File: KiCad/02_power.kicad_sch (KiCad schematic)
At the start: 0 parts

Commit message: Update power scheme
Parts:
- added C100, C101, C102, C103, C203, C204: 2.2uF, Capacitor_SMD:C_0603_1608Metric, symbol Device:C
- added C104: DNP, Capacitor_SMD:C_0603_1608Metric, symbol Device:C
- added C205, C206: 22uF, Capacitor_SMD:C_0603_1608Metric, symbol Device:C
- added C207, C208: 100nF, Capacitor_SMD:C_0603_1608Metric, symbol Device:C
- added C209, C500: 10uF, Capacitor_SMD:C_0603_1608Metric, symbol Device:C
- added D100, D101: LED, LED_SMD:LED_0603_1608Metric, symbol Device:LED
- added D201, D202, D203: 1N5819HW-7-F, Diode_SMD:D_SOD-123, symbol Device:D_Schottky
- added F100, F101, F201: 3A, Fuse:Fuse_0805_2012Metric, symbol Device:Polyfuse
- added FB100, FB101, FB201: 120R, Fuse:Fuse_0603_1608Metric, symbol Device:FerriteBead
- added J100: Barrel_Jack_Switch_Pin3Ring, Connector_BarrelJack:BarrelJack_GCT_DCJ200-10-A_Horizontal, symbol Connector:Barrel_Jack_Switch_Pin3Ring
- added L101: 15uH, esp32_s3_weather_webserver:MWSA0603S, symbol Device:L
- added R100: 100kR, Resistor_SMD:R_0805_2012Metric, symbol Device:R
- added R101: 22kR, Resistor_SMD:R_0805_2012Metric, symbol Device:R
- added R102, R201: 510R, Resistor_SMD:R_0402_1005Metric, symbol Device:R
- added U100: TLV62569DBV, Package_TO_SOT_SMD:SOT-23-5, symbol Regulator_Switching:TLV62569DBV
- added U201: AMS1117-3.3, Package_TO_SOT_SMD:SOT-223-3_TabPin2, symbol Regulator_Linear:AMS1117-3.3
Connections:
- new net +3V3: C208.1, C209.1, R201.2, U201.2 (VO)
- new net +3V3_PER: C104.1, C206.1, L101.2, R100.2, R102.2
- new net +5V: C205.1, C207.1, C500.1, D201.1 (K), D202.1 (K), D203.1 (K), U100.1 (EN), U100.4 (VIN), U201.3 (VI)
- new net +5V_IN: F100.1, J100.1
- new net +5V_IN_FILT: C101.1, D201.2 (A), FB100.1
- new net +5V_IN_FUSE: C100.1, F100.2, FB100.2
- new net +VCC_USB2UART_FILT: C103.1, D202.2 (A), FB101.1
- new net +VCC_USB2UART_FUSE: C102.1, F101.2, FB101.2
- new net +VCC_USB_FILT: C204.1, D203.2 (A), FB201.1
- new net +VCC_USB_FUSE: C203.1, F201.2, FB201.2
- new net BUCK_FB: C104.2, R100.1, R101.2, U100.5 (FB)
- new net BUCK_SW: L101.1, U100.3 (SW)
- new net GND: C100.2, C101.2, C102.2, C103.2, C203.2, C204.2, C205.2, C206.2, C207.2, C208.2, C209.2, C500.2, D100.1 (K), D101.1 (K), J100.2, J100.3, R101.1, U100.2 (GND), U201.1 (GND)
- new net LED_3V3_A: D100.2 (A), R201.1
- new net LED_3V3_PER_A: D101.2 (A), R102.1
- new net USB2UART_VBUS: F101.1
- new net USB_VBUS: F201.1
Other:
- note added: "I(load)=0.25A max"
- note added: "Power indication"
- note added: "Power input"
- note added: "Powering ESP32"
- note added: "Powering Peripherals"
- note added: "V(out)=0.6*(1+100k/22k)=3.327V"
- note added: "WEBENCH Tools"
- note added: "[2] Power"
- note added: "f(sw)=1.5MHz"

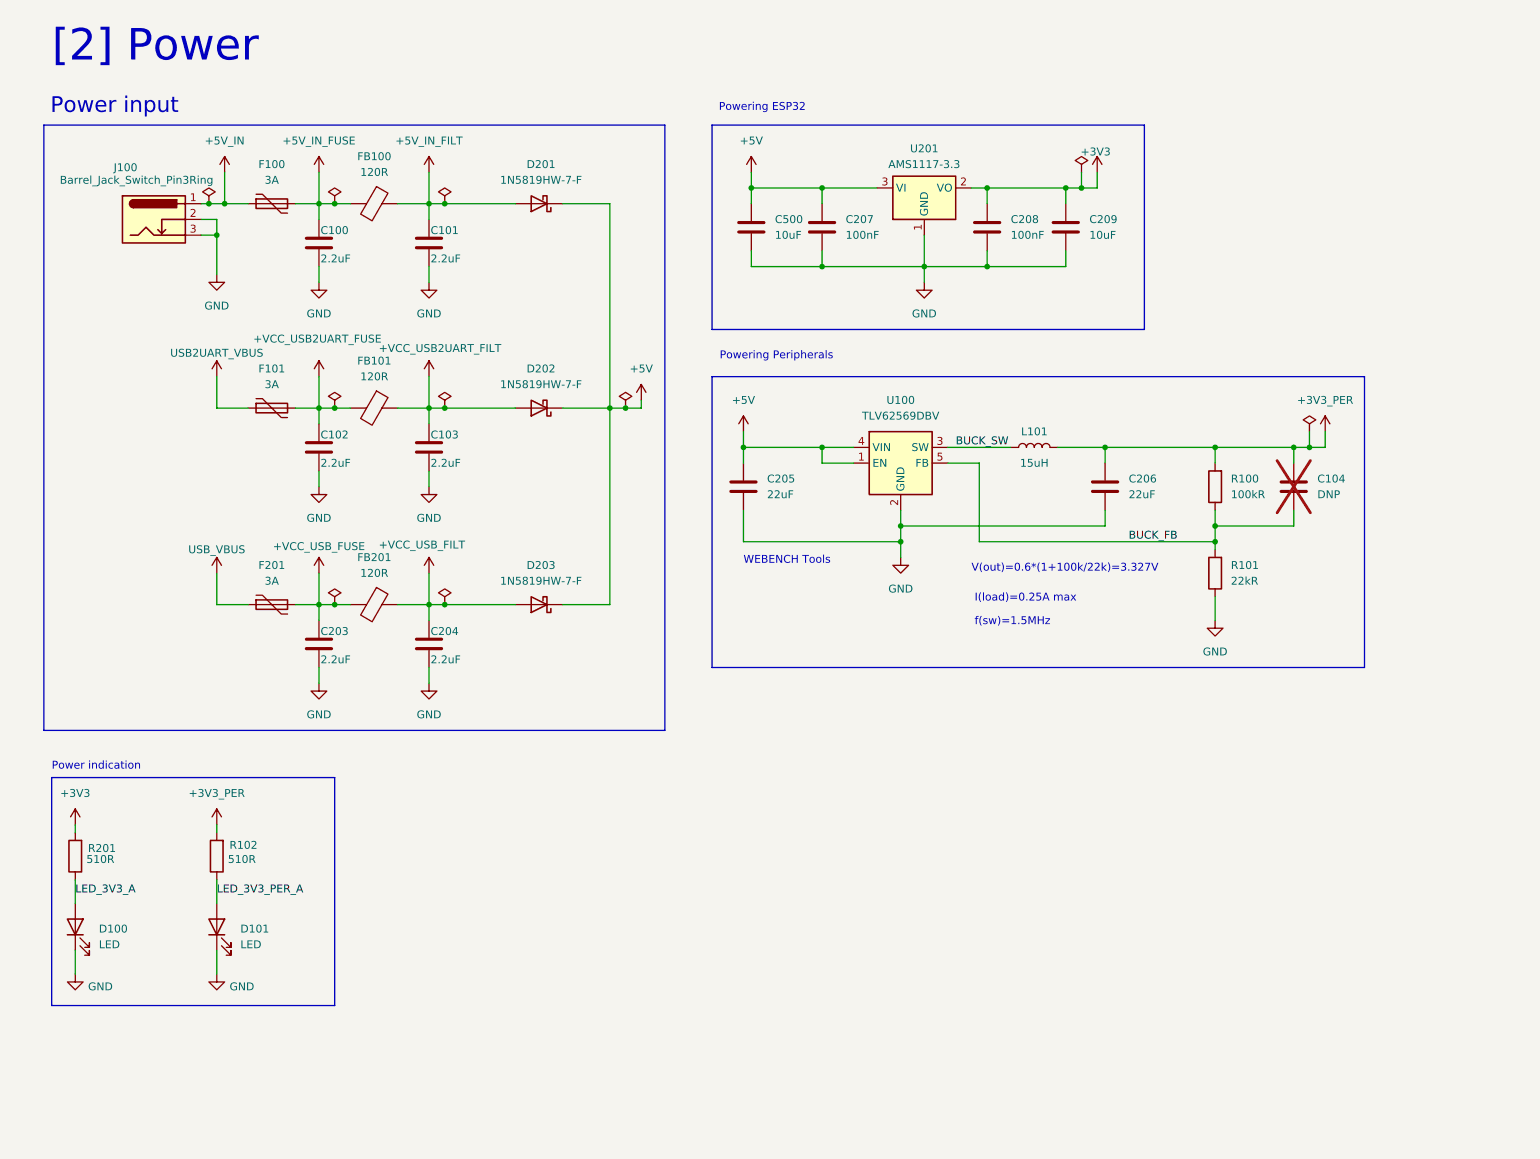
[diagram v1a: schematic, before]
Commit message: Add analog sensors
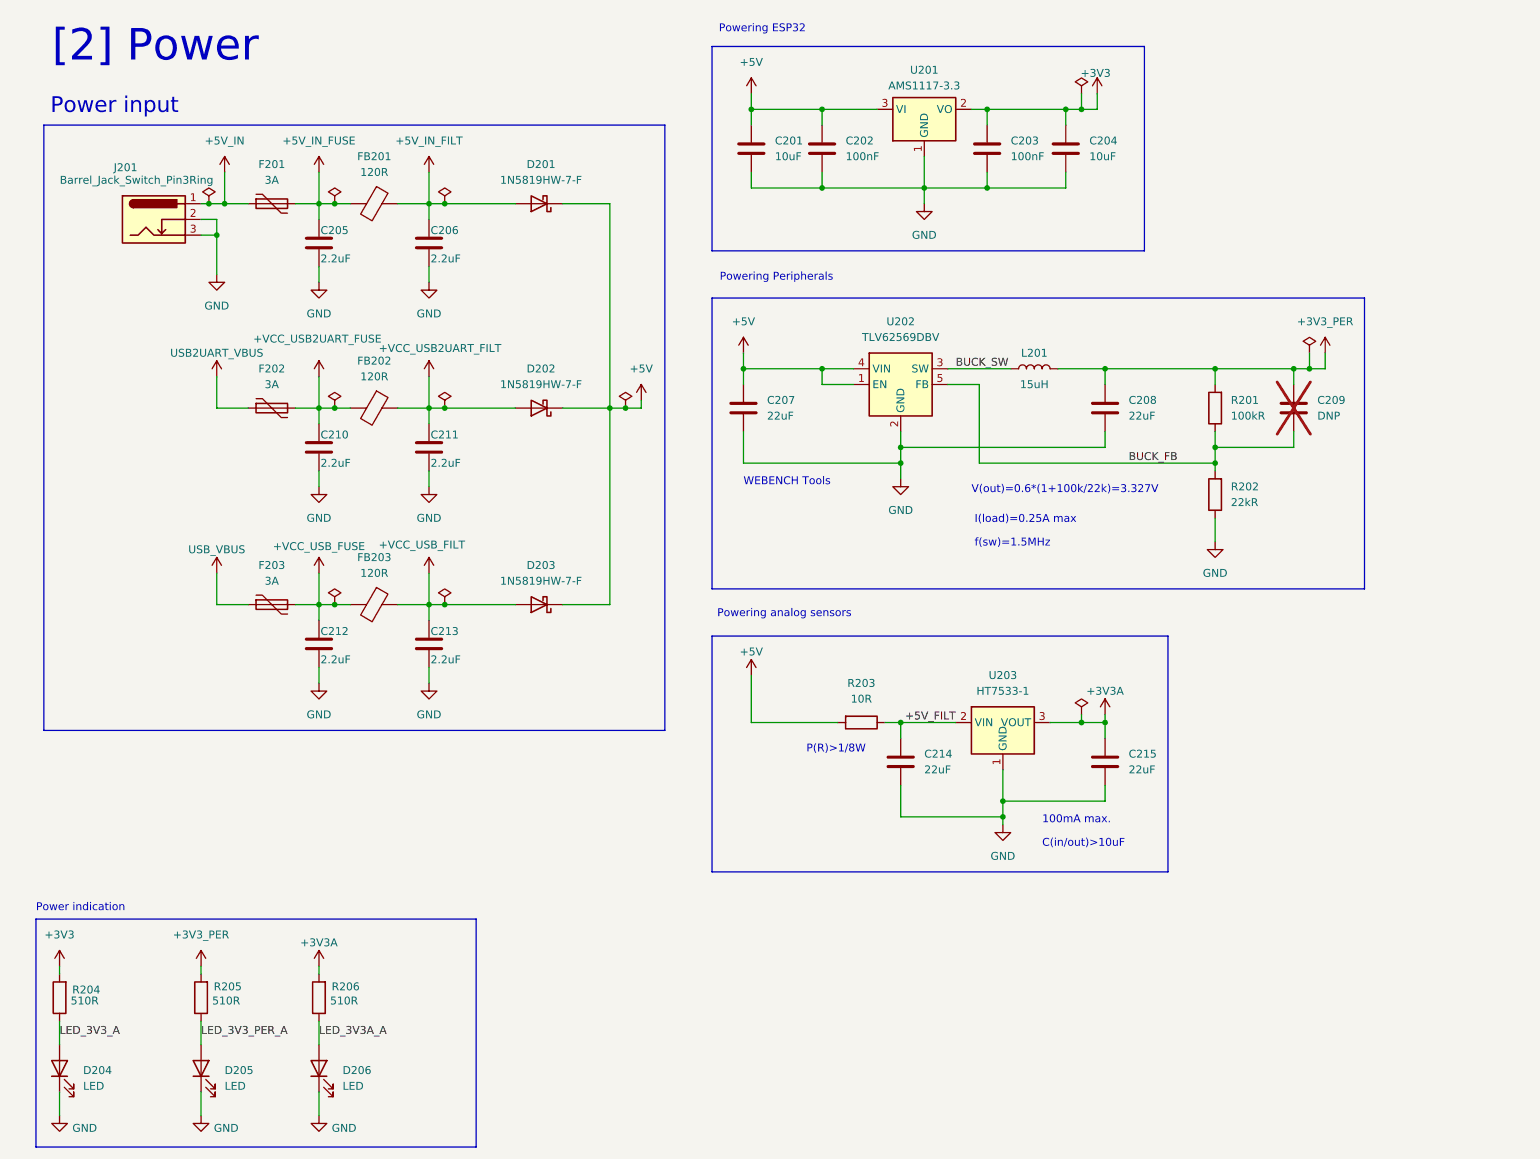
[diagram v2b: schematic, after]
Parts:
- added C214, C215: 22uF, Capacitor_SMD:C_0805_2012Metric, symbol Device:C
- added D206: LED, LED_SMD:LED_0603_1608Metric, symbol Device:LED
- added R203: 10R, Resistor_SMD:R_0805_2012Metric, symbol Device:R
- added R206: 510R, Resistor_SMD:R_0402_1005Metric, symbol Device:R
- added U203: HT7533-1, Package_TO_SOT_SMD:SOT-89-3, symbol Regulator_Linear:HT75xx-1-SOT89
- renumbered C500 to C201, C207 to C202, C208 to C203, C209 to C204, C100 to C205, C101 to C206, C205 to C207, C206 to C208, C104 to C209, C102 to C210, C103 to C211, C203 to C212, C204 to C213, D100 to D204, D101 to D205, F100 to F201, F101 to F202, F201 to F203, FB100 to FB201, FB101 to FB202, FB201 to FB203, J100 to J201, L101 to L201, R100 to R201, R101 to R202, R201 to R204, R102 to R205, U100 to U202
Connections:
- net +5V: now also R203.2
- net GND: now also C214.2, C215.2, D206.1 (K), U203.1 (GND)
- new net +3V3A: C215.1, R206.2, U203.3 (VOUT)
- new net +5V_FILT: C214.1, R203.1, U203.2 (VIN)
- new net LED_3V3A_A: D206.2 (A), R206.1
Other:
- note added: "100mA max."
- note added: "C(in/out)>10uF"
- note added: "P(R)>1/8W"
- note added: "Powering analog sensors"
- moved on the sheet: C201, C202, C203, C204, C207, C208, C209, D204, D205, L201, R201, R202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

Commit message: First scheme version
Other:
- moved on the sheet: C214, C215, R203, U203

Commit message: Firmware refactoring. Beginning
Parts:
- added D1: LED, LED_SMD:LED_0603_1608Metric, symbol Device:LED
- added D501, D502, D503, D504: WS2812B, LED_SMD:LED_WS2812B_PLCC4_5.0x5.0mm_P3.2mm, symbol LED:WS2812B
- added R3: 510R, Resistor_SMD:R_0402_1005Metric, symbol Device:R
- added R512: 0R, Resistor_SMD:R_0805_2012Metric, symbol Device:R
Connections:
- net +5V: now also D501.1 (VDD), D502.1 (VDD), D503.1 (VDD), D504.1 (VDD)
- net GND: now also D1.1 (K), D501.3 (VSS), D502.3 (VSS), D503.3 (VSS), D504.3 (VSS)
- new net: D501.2 (DOUT), D502.4 (DIN)
- new net: D501.4 (DIN), R512.1
- new net: D503.2 (DOUT), D504.4 (DIN)
- new net: D502.2 (DOUT), D503.4 (DIN)
- new net LED_ONBOARD_A: D1.2 (A), R3.1
- new net ONBOARD_LED: R3.2
- new net WS2812_RGB_STRIP: R512.2
- no-connect marks 0 -> 1
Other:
- note added: "RGB strip"
- moved on the sheet: D204, D205, D206, R204, R205, R206

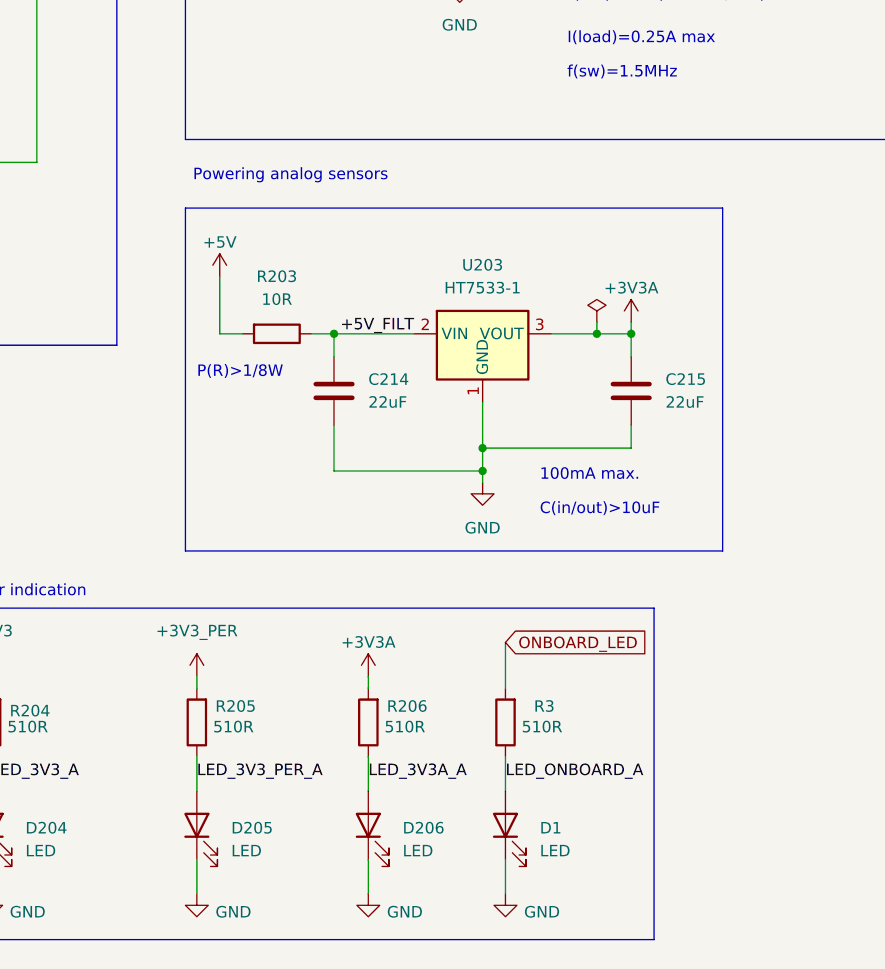
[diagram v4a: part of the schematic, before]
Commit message: Remove 3V3A power chain
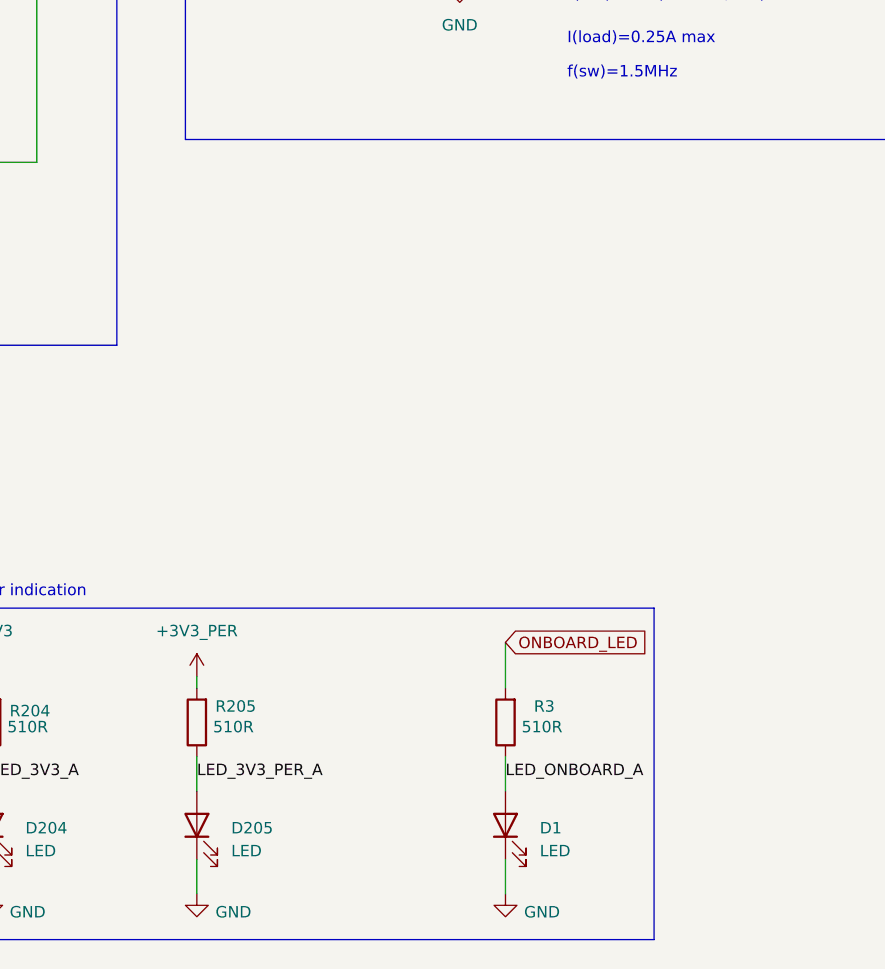
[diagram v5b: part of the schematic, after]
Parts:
- removed C214, C215: 22uF, Capacitor_SMD:C_0805_2012Metric, symbol Device:C
- removed D206: LED, LED_SMD:LED_0603_1608Metric, symbol Device:LED
- removed R203: 10R, Resistor_SMD:R_0805_2012Metric, symbol Device:R
- removed R206: 510R, Resistor_SMD:R_0402_1005Metric, symbol Device:R
- removed U203: HT7533-1, Package_TO_SOT_SMD:SOT-89-3, symbol Regulator_Linear:HT75xx-1-SOT89
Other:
- note removed: "100mA max."
- note removed: "C(in/out)>10uF"
- note removed: "P(R)>1/8W"
- note removed: "Powering analog sensors"

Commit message: BOM updates
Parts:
- D201, D202, D203: Manufacturer (none) -> DIODES; Manufacturer Part Number (none) -> 1N5819HW-7-F
- D501, D502, D503, D504: Manufacturer (none) -> Worldsemi; Manufacturer Part Number (none) -> WS2812B-B/W
- R204, R205, R3: footprint Resistor_SMD:R_0402_1005Metric -> Resistor_SMD:R_0805_2012Metric; Manufacturer Part Number 0402WGF5100TCE -> 0805W8F5100T5E
- U201: Manufacturer (none) -> Advanced Monolithic Systems; Manufacturer Part Number (none) -> AMS1117-3.3
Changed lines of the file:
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@@
 			)
 		)
+		(property "Manufacturer" "Advanced Monolithic Systems"
+			(at 157.48 29.21 0)
+			(effects
+				(font
+					(size 1.27 1.27)
+				)
+				(hide yes)
+			)
+		)
+		(property "Manufacturer Part Number" "AMS1117-3.3"
+			(at 157.48 29.21 0)
+			(effects
+				(font
+					(size 1.27 1.27)
+				)
+				(hide yes)
+			)
+		)
 		(pin "3"
 		)
@@
 			)
 		)
+		(property "Manufacturer" "Worldsemi"
+			(at 30.48 179.07 0)
+			(effects
+				(font
+					(size 1.27 1.27)
+				)
+				(hide yes)
+			)
+		)
+		(property "Manufacturer Part Number" "WS2812B-B/W"
+			(at 30.48 179.07 0)
+			(effects
+				(font
+					(size 1.27 1.27)
+				)
+				(hide yes)
+			)
+		)
 		(pin "3"
 		)
@@
 			)
 		)
+		(property "Manufacturer" "Worldsemi"
+			(at 66.04 179.07 0)
+			(effects
+				(font
+					(size 1.27 1.27)
+				)
+				(hide yes)
+			)
+		)
+		(property "Manufacturer Part Number" "WS2812B-B/W"
+			(at 66.04 179.07 0)
+			(effects
+				(font
+					(size 1.27 1.27)
+				)
+				(hide yes)
+			)
+		)
 		(pin "3"
 		)
@@
 			)
 		)
-		(property "Footprint" "Resistor_SMD:R_0402_1005Metric"
+		(property "Footprint" "Resistor_SMD:R_0805_2012Metric"
 			(at 126.238 171.45 90)
 			(effects
@@
 			)
 		)
-		(property "Manufacturer Part Number" "0402WGF5100TCE"
+		(property "Manufacturer Part Number" "0805W8F5100T5E"
 			(at 124.46 171.45 0)
 			(effects
@@
 			)
 		)
+		(property "Manufacturer" "DIODES"
+			(at 95.25 109.22 0)
+			(effects
+				(font
+					(size 1.27 1.27)
+				)
+				(hide yes)
+			)
+		)
+		(property "Manufacturer Part Number" "1N5819HW-7-F"
+			(at 95.25 109.22 0)
+			(effects
+				(font
+					(size 1.27 1.27)
+				)
+				(hide yes)
+			)
+		)
 		(pin "2"
 		)
@@
 			)
 		)
-		(property "Footprint" "Resistor_SMD:R_0402_1005Metric"
+		(property "Footprint" "Resistor_SMD:R_0805_2012Metric"
 			(at 103.378 171.45 90)
 			(effects
@@
 			)
 		)
-		(property "Manufacturer Part Number" "0402WGF5100TCE"
+		(property "Manufacturer Part Number" "0805W8F5100T5E"
 			(at 101.6 171.45 0)
 			(effects
@@
 			)
 		)
+		(property "Manufacturer" "DIODES"
+			(at 95.25 77.47 0)
+			(effects
+				(font
+					(size 1.27 1.27)
+				)
+				(hide yes)
+			)
+		)
+		(property "Manufacturer Part Number" "1N5819HW-7-F"
+			(at 95.25 77.47 0)
+			(effects
+				(font
+					(size 1.27 1.27)
+				)
+				(hide yes)
+			)
+		)
 		(pin "2"
 		)
@@
 			)
 		)
+		(property "Manufacturer" "Worldsemi"
+			(at 83.82 179.07 0)
+			(effects
+				(font
+					(size 1.27 1.27)
+				)
+				(hide yes)
+			)
+		)
+		(property "Manufacturer Part Number" "WS2812B-B/W"
+			(at 83.82 179.07 0)
+			(effects
+				(font
+					(size 1.27 1.27)
+				)
+				(hide yes)
+			)
+		)
 		(pin "3"
 		)
@@
 			)
 		)
+		(property "Manufacturer" "Worldsemi"
+			(at 48.26 179.07 0)
+			(effects
+				(font
+					(size 1.27 1.27)
+				)
+				(hide yes)
+			)
+		)
+		(property "Manufacturer Part Number" "WS2812B-B/W"
+			(at 48.26 179.07 0)
+			(effects
+				(font
+					(size 1.27 1.27)
+				)
+				(hide yes)
+			)
+		)
 		(pin "3"
 		)
@@
 			)
 		)
+		(property "Manufacturer" "DIODES"
+			(at 95.25 44.45 0)
+			(effects
+				(font
+					(size 1.27 1.27)
+				)
+				(hide yes)
+			)
+		)
+		(property "Manufacturer Part Number" "1N5819HW-7-F"
+			(at 95.25 44.45 0)
+			(effects
+				(font
+					(size 1.27 1.27)
+				)
+				(hide yes)
+			)
+		)
 		(pin "2"
 		)
@@
 			)
 		)
-		(property "Footprint" "Resistor_SMD:R_0402_1005Metric"
+		(property "Footprint" "Resistor_SMD:R_0805_2012Metric"
 			(at 160.528 171.45 90)
 			(effects
@@
 			)
 		)
-		(property "Manufacturer Part Number" "0402WGF5100TCE"
+		(property "Manufacturer Part Number" "0805W8F5100T5E"
 			(at 158.75 171.45 0)
 			(effects

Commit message: BOM updates. First layout
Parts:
- C202, C203: footprint Capacitor_SMD:C_0603_1608Metric -> Capacitor_SMD:C_0402_1005Metric; Manufacturer Part Number CL10B104KB8NNNC -> CL05B104KO5NNNC
- R201: footprint Resistor_SMD:R_0805_2012Metric -> Resistor_SMD:R_0402_1005Metric; Manufacturer Part Number 0805W8F1003T5E -> 0402WGF1003TCE
- R202: footprint Resistor_SMD:R_0805_2012Metric -> Resistor_SMD:R_0402_1005Metric; Manufacturer Part Number 0805W8F2202T5E -> 0402WGF2202TCE
- R204, R205: footprint Resistor_SMD:R_0805_2012Metric -> Resistor_SMD:R_0402_1005Metric; Manufacturer Part Number 0805W8F5100T5E -> 0402WGF5100TCE
- R206: renamed from R3; footprint Resistor_SMD:R_0805_2012Metric -> Resistor_SMD:R_0402_1005Metric; Manufacturer Part Number 0805W8F5100T5E -> 0402WGF5100TCE
- renumbered D501 to D204, D502 to D205, D503 to D206, D504 to D207, D204 to D208, D205 to D209, D1 to D210, R512 to R203
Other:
- moved on the sheet: D208, D209, D210, R204, R205, R206
